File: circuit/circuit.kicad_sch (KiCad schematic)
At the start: 26 parts, among them SW101 Pedal_1, SW102 Pedal_2, SW103 Pedal_3, SW104 Pedal_4, SW105 Pedal_5, SW106 Pedal_6, SW107 Pedal_7, SW108 Pedal_8, SW109 Program, SW110 Preset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

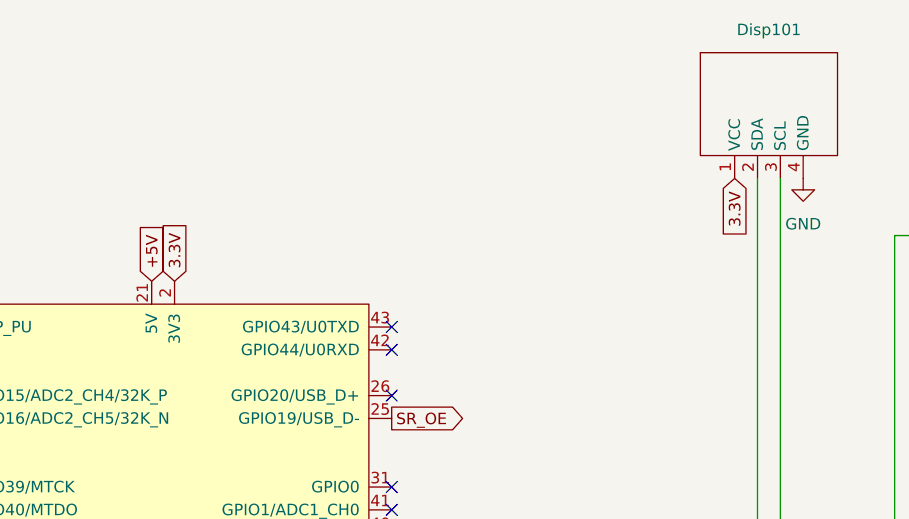
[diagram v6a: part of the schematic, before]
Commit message: Fine tuning of circuit
Added jumper to select voltage of display, changed 3.3V regulator from SMD to TO-220 to simplify DIY builds.
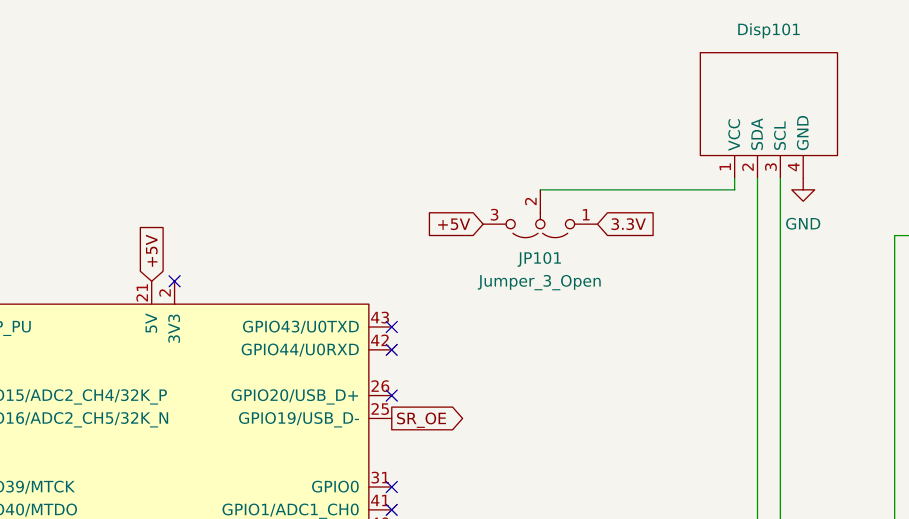
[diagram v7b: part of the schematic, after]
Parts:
- added JP101: Jumper_3_Open, Connector_PinSocket_2.54mm:PinSocket_1x03_P2.54mm_Vertical, symbol Jumper:Jumper_3_Open
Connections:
- net +5V: now also JP101.3 (B)
- net 3.3V: now also JP101.1 (A); no longer Disp101.1 (VCC), U101.1 (3V3), U101.2 (3V3)
- new net: Disp101.1 (VCC), JP101.2 (C)
- new net: U101.1 (3V3), U101.2 (3V3)
- no-connect marks 20 -> 21
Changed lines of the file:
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@@
+	)
+	(no_connect
+		(at 156.21 55.88)
 	)
 	(no_connect
@@
 	(wire
 		(pts
+			(xy 196.85 45.72) (xy 218.44 45.72)
+		)
+		(stroke
+			(width 0)
+			(type default)
+		)
+	)
+	(wire
+		(pts
 			(xy 203.2 109.22) (xy 203.2 127)
 		)
@@
 		)
 	)
+	(wire
+		(pts
+			(xy 218.44 45.72) (xy 218.44 44.45)
+		)
+		(stroke
+			(width 0)
+			(type default)
+		)
+	)
 	(bus
 		(pts
@@
 			(width 0)
 			(type default)
-		)
-	)
-	(global_label "3.3V"
-		(shape input)
-		(at 218.44 44.45 270)
-		(fields_autoplaced yes)
-		(effects
-			(font
-				(size 1.27 1.27)
-			)
-			(justify right)
-		)
-		(property "Intersheetrefs" "${INTERSHEET_REFS}"
-			(at 218.44 51.5476 90)
-			(effects
-				(font
-					(size 1.27 1.27)
-				)
-				(justify right)
-				(hide yes)
-			)
-		)
-	)
-	(global_label "3.3V"
-		(shape input)
-		(at 156.21 55.88 90)
-		(fields_autoplaced yes)
-		(effects
-			(font
-				(size 1.27 1.27)
-			)
-			(justify left)
-		)
-		(property "Intersheetrefs" "${INTERSHEET_REFS}"
-			(at 156.21 48.7824 90)
-			(effects
-				(font
-					(size 1.27 1.27)
-				)
-				(justify left)
-				(hide yes)
-			)
 		)
 	)
@@
 		)
 	)
+	(global_label "3.3V"
+		(shape input)
+		(at 203.2 49.53 0)
+		(fields_autoplaced yes)
+		(effects
+			(font
+				(size 1.27 1.27)
+			)
+			(justify left)
+		)
+		(property "Intersheetrefs" "${INTERSHEET_REFS}"
+			(at 210.2976 49.53 0)
+			(effects
+				(font
+					(size 1.27 1.27)
+				)
+				(justify left)
+				(hide yes)
+			)
+		)
+	)
 	(global_label "MATRIX_SR_DS"
 		(shape output)
@@
 		(property "Intersheetrefs" "${INTERSHEET_REFS}"
 			(at 171.4282 71.12 0)
+			(effects
+				(font
+					(size 1.27 1.27)
+				)
+				(justify right)
+				(hide yes)
+			)
+		)
+	)
+	(global_label "+5V"
+		(shape input)
+		(at 190.5 49.53 180)
+		(fields_autoplaced yes)
+		(effects
+			(font
+				(size 1.27 1.27)
+			)
+			(justify right)
+		)
+		(property "Intersheetrefs" "${INTERSHEET_REFS}"
+			(at 183.6443 49.53 0)
 			(effects
 				(font
@@
 					(unit 1)
 				)
+			)
+		)
+	)
+	(symbol
+		(lib_id "Jumper:Jumper_3_Open")
+		(at 196.85 49.53 180)
+		(unit 1)
+		(exclude_from_sim no)
+		(in_bom no)
+		(on_board yes)
+		(dnp no)
+		(fields_autoplaced yes)
+		(property "Reference" "JP101"
+			(at 196.85 53.34 0)
+			(effects
+				(font
+					(size 1.27 1.27)
+				)
+			)
+		)
+		(property "Value" "Jumper_3_Open"
+			(at 196.85 55.88 0)
+			(effects
+				(font
+					(size 1.27 1.27)
+				)
+			)
+		)
+		(property "Footprint" "Connector_PinSocket_2.54mm:PinSocket_1x03_P2.54mm_Vertical"
+			(at 196.85 49.53 0)
+			(effects
+				(font
+					(size 1.27 1.27)
+				)
+				(hide yes)
+			)
+		)
+		(property "Datasheet" "~"
+			(at 196.85 49.53 0)
+			(effects
+				(font
+					(size 1.27 1.27)
+				)
+				(hide yes)
+			)
+		)
+		(property "Description" "Jumper, 3-pole, both open"
+			(at 196.85 49.53 0)
+			(effects
+				(font
+					(size 1.27 1.27)
+				)
+				(hide yes)
+			)
+		)
+		(pin "2"
+		)
+		(pin "3"
+		)
+		(pin "1"
+		)
+		(instances
+			(project ""
+				(path "/420e3d7a-6c9a-4806-b4be-05d56aeb21de"
+					(reference "JP101")
+					(unit 1)
+				)

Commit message: Added ferrite beads and tweaked PCB
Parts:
- C101, C102, C103, C104, C105, C106, C107, C108, C109, C110: footprint Capacitor_THT:C_Axial_L3.8mm_D2.6mm_P7.50mm_Horizontal -> Capacitor_THT:C_Disc_D3.0mm_W2.0mm_P2.50mm
- D101, SW101, SW102, SW103, SW104, SW105, SW106, SW107, SW108, SW109, SW110: footprint Connector_Wire:SolderWire-0.1sqmm_1x02_P3.6mm_D0.4mm_OD1mm -> Connector_PinHeader_2.54mm:PinHeader_1x02_P2.54mm_Vertical
- Disp101: footprint Connector_PinHeader_1.00mm:PinHeader_1x04_P1.00mm_Vertical -> Connector_PinHeader_2.54mm:PinHeader_1x04_P2.54mm_Vertical
- R101: footprint Resistor_THT:R_Axial_DIN0204_L3.6mm_D1.6mm_P5.08mm_Horizontal -> Resistor_THT:R_Axial_DIN0207_L6.3mm_D2.5mm_P7.62mm_Horizontal
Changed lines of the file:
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@@
 			)
 		)
-		(property "Footprint" "Connector_Wire:SolderWire-0.1sqmm_1x02_P3.6mm_D0.4mm_OD1mm"
+		(property "Footprint" "Connector_PinHeader_2.54mm:PinHeader_1x02_P2.54mm_Vertical"
 			(at 304.8 71.12 0)
 			(effects
@@
 			)
 		)
-		(property "Description" "Push button switch, generic, two pins"
+		(property "Description" ""
 			(at 304.8 76.2 0)
 			(effects
@@
 			)
 		)
-		(property "Footprint" "Resistor_THT:R_Axial_DIN0204_L3.6mm_D1.6mm_P5.08mm_Horizontal"
+		(property "Footprint" "Resistor_THT:R_Axial_DIN0207_L6.3mm_D2.5mm_P7.62mm_Horizontal"
 			(at 43.18 63.5 0)
 			(effects
@@
 			)
 		)
-		(property "Footprint" "Capacitor_THT:C_Axial_L3.8mm_D2.6mm_P7.50mm_Horizontal"
+		(property "Footprint" "Capacitor_THT:C_Disc_D3.0mm_W2.0mm_P2.50mm"
 			(at 330.2 110.49 0)
 			(effects
@@
 			)
 		)
-		(property "Footprint" "Capacitor_THT:C_Axial_L3.8mm_D2.6mm_P7.50mm_Horizontal"
+		(property "Footprint" "Capacitor_THT:C_Disc_D3.0mm_W2.0mm_P2.50mm"
 			(at 292.1 135.89 0)
 			(effects
@@
 			)
 		)
-		(property "Footprint" "Connector_PinHeader_1.00mm:PinHeader_1x04_P1.00mm_Vertical"
+		(property "Footprint" "Connector_PinHeader_2.54mm:PinHeader_1x04_P2.54mm_Vertical"
 			(at 222.25 35.56 0)
 			(effects
@@
 			)
 		)
-		(property "Footprint" "Connector_Wire:SolderWire-0.1sqmm_1x02_P3.6mm_D0.4mm_OD1mm"
+		(property "Footprint" "Connector_PinHeader_2.54mm:PinHeader_1x02_P2.54mm_Vertical"
 			(at 279.4 109.22 0)
 			(effects
@@
 			)
 		)
-		(property "Description" "Push button switch, generic, two pins"
+		(property "Description" ""
 			(at 279.4 114.3 0)
 			(effects
@@
 			)
 		)
-		(property "Footprint" "Connector_Wire:SolderWire-0.1sqmm_1x02_P3.6mm_D0.4mm_OD1mm"
+		(property "Footprint" "Connector_PinHeader_2.54mm:PinHeader_1x02_P2.54mm_Vertical"
 			(at 330.2 96.52 0)
 			(effects
@@
 			)
 		)
-		(property "Description" "Push button switch, generic, two pins"
+		(property "Description" ""
 			(at 330.2 101.6 0)
 			(effects
@@
 			)
 		)
-		(property "Footprint" "Capacitor_THT:C_Axial_L3.8mm_D2.6mm_P7.50mm_Horizontal"
+		(property "Footprint" "Capacitor_THT:C_Disc_D3.0mm_W2.0mm_P2.50mm"
 			(at 279.4 123.19 0)
 			(effects
@@
 			)
 		)
-		(property "Footprint" "Connector_Wire:SolderWire-0.1sqmm_1x02_P3.6mm_D0.4mm_OD1mm"
+		(property "Footprint" "Connector_PinHeader_2.54mm:PinHeader_1x02_P2.54mm_Vertical"
 			(at 317.5 147.32 0)
 			(effects
@@
 			)
 		)
-		(property "Description" "Push button switch, generic, two pins"
+		(property "Description" ""
 			(at 317.5 152.4 0)
 			(effects
@@
 			)
 		)
-		(property "Footprint" "Capacitor_THT:C_Axial_L3.8mm_D2.6mm_P7.50mm_Horizontal"
+		(property "Footprint" "Capacitor_THT:C_Disc_D3.0mm_W2.0mm_P2.50mm"
 			(at 304.8 85.09 0)
 			(effects
@@
 			)
 		)
-		(property "Footprint" "Connector_Wire:SolderWire-0.1sqmm_1x02_P3.6mm_D0.4mm_OD1mm"
+		(property "Footprint" "Connector_PinHeader_2.54mm:PinHeader_1x02_P2.54mm_Vertical"
 			(at 292.1 58.42 0)
 			(effects
@@
 			)
 		)
-		(property "Description" "Push button switch, generic, two pins"
+		(property "Description" ""
 			(at 292.1 63.5 0)
 			(effects
@@
 			)
 		)
-		(property "Footprint" "Connector_Wire:SolderWire-0.1sqmm_1x02_P3.6mm_D0.4mm_OD1mm"
+		(property "Footprint" "Connector_PinHeader_2.54mm:PinHeader_1x02_P2.54mm_Vertical"
 			(at 304.8 134.62 0)
 			(effects
@@
 			)
 		)
-		(property "Description" "Push button switch, generic, two pins"
+		(property "Description" ""
 			(at 304.8 139.7 0)
 			(effects
@@
 			)
 		)
-		(property "Footprint" "Connector_Wire:SolderWire-0.1sqmm_1x02_P3.6mm_D0.4mm_OD1mm"
+		(property "Footprint" "Connector_PinHeader_2.54mm:PinHeader_1x02_P2.54mm_Vertical"
 			(at 330.2 160.02 0)
 			(effects
@@
 			)
 		)
-		(property "Description" "Push button switch, generic, two pins"
+		(property "Description" ""
 			(at 330.2 165.1 0)
 			(effects
@@
 			)
 		)
-		(property "Footprint" "Capacitor_THT:C_Axial_L3.8mm_D2.6mm_P7.50mm_Horizontal"
+		(property "Footprint" "Capacitor_THT:C_Disc_D3.0mm_W2.0mm_P2.50mm"
 			(at 317.5 161.29 0)
 			(effects
@@
 			)
 		)
-		(property "Footprint" "Capacitor_THT:C_Axial_L3.8mm_D2.6mm_P7.50mm_Horizontal"
+		(property "Footprint" "Capacitor_THT:C_Disc_D3.0mm_W2.0mm_P2.50mm"
 			(at 304.8 148.59 0)
 			(effects
@@
 			)
 		)
-		(property "Footprint" "Connector_Wire:SolderWire-0.1sqmm_1x02_P3.6mm_D0.4mm_OD1mm"
+		(property "Footprint" "Connector_PinHeader_2.54mm:PinHeader_1x02_P2.54mm_Vertical"
 			(at 317.5 83.82 0)
 			(effects
@@
 			)
 		)
-		(property "Description" "Push button switch, generic, two pins"
+		(property "Description" ""
 			(at 317.5 88.9 0)
 			(effects
@@
 			)
 		)
-		(property "Footprint" "Capacitor_THT:C_Axial_L3.8mm_D2.6mm_P7.50mm_Horizontal"
+		(property "Footprint" "Capacitor_THT:C_Disc_D3.0mm_W2.0mm_P2.50mm"
 			(at 330.2 173.99 0)
 			(effects
@@
 			)
 		)
-		(property "Footprint" "Connector_Wire:SolderWire-0.1sqmm_1x02_P3.6mm_D0.4mm_OD1mm"
+		(property "Footprint" "Connector_PinHeader_2.54mm:PinHeader_1x02_P2.54mm_Vertical"
 			(at 58.42 63.5 0)
 			(effects
@@
 			)
 		)
-		(property "Footprint" "Connector_Wire:SolderWire-0.1sqmm_1x02_P3.6mm_D0.4mm_OD1mm"
+		(property "Footprint" "Connector_PinHeader_2.54mm:PinHeader_1x02_P2.54mm_Vertical"
 			(at 279.4 45.72 0)
 			(effects
@@
 			)
 		)
-		(property "Description" "Push button switch, generic, two pins"
+		(property "Description" ""
 			(at 279.4 50.8 0)
 			(effects
@@
 			)
 		)
-		(property "Footprint" "Capacitor_THT:C_Axial_L3.8mm_D2.6mm_P7.50mm_Horizontal"
+		(property "Footprint" "Capacitor_THT:C_Disc_D3.0mm_W2.0mm_P2.50mm"
 			(at 317.5 97.79 0)
 			(effects
@@
 			)
 		)
-		(property "Footprint" "Capacitor_THT:C_Axial_L3.8mm_D2.6mm_P7.50mm_Horizontal"
+		(property "Footprint" "Capacitor_THT:C_Disc_D3.0mm_W2.0mm_P2.50mm"
 			(at 279.4 59.69 0)
 			(effects
@@
 			)
 		)
-		(property "Footprint" "Capacitor_THT:C_Axial_L3.8mm_D2.6mm_P7.50mm_Horizontal"
+		(property "Footprint" "Capacitor_THT:C_Disc_D3.0mm_W2.0mm_P2.50mm"
 			(at 292.1 72.39 0)
 			(effects
@@
 			)
 		)
-		(property "Footprint" "Connector_Wire:SolderWire-0.1sqmm_1x02_P3.6mm_D0.4mm_OD1mm"
+		(property "Footprint" "Connector_PinHeader_2.54mm:PinHeader_1x02_P2.54mm_Vertical"
 			(at 292.1 121.92 0)
 			(effects
@@
 			)
 		)
-		(property "Description" "Push button switch, generic, two pins"
+		(property "Description" ""
 			(at 292.1 127 0)
 			(effects
